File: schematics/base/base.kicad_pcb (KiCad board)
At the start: 2 copper layers, 96.5 x 96.5 mm, 41 parts, among them J1 Bionic_ZIF_Socket_48pin, J2 USB_C_USB2.0_16P, J3 USB_C_USB2.0_16P, J4 P1/P2, J5 P3/P4, J6 P5, J7 P6, SW1 USR_SW, U1 TXS0108EPW, U2 TXS0108EPW, U3 TXS0108EPW, U4 TXS0108EPW, U5 TXS0108EPW, U6 SN74ACT1071DR, U7 SN74ACT1071DR

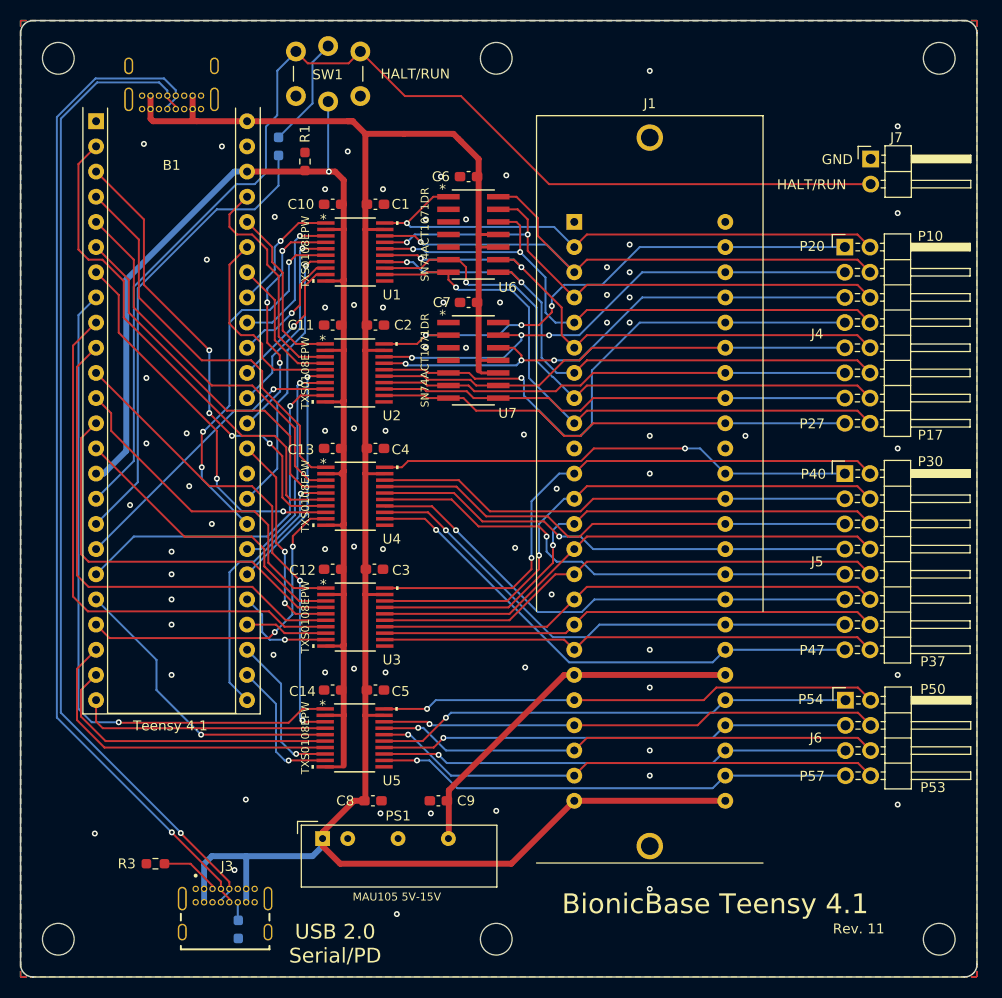
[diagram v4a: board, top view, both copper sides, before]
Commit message: [base] 4 Layers
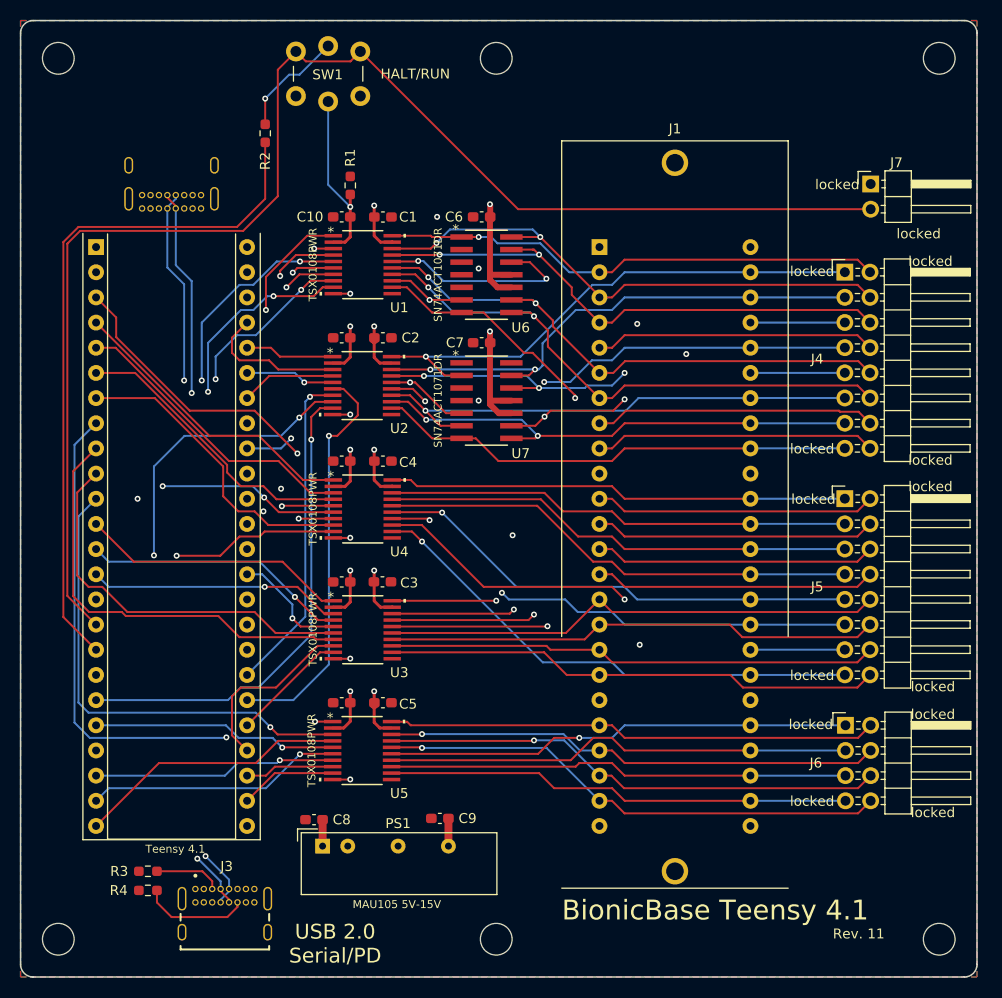
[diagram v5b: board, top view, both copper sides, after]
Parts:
- R2, R4: moved to F.Cu
- moved B1 12.7 mm to (80.7, 64.9)
- moved J2 10.0 mm to (88.3, 56.7)
- moved R4 9.93 mm to (85.9, 129.8), turned to 180 degrees
- moved C8 6.24 mm to (102.7, 122.7), turned to 180 degrees
- moved R1 5.17 mm to (106.3, 58.7)
- moved U7 4.27 mm to (120.1, 80.4)
- moved C7 4.27 mm to (119.6, 74.6)
- moved U6 4.27 mm to (120.1, 67.7)
- moved C6 4.27 mm to (119.6, 61.9)
- moved J1 3.59 mm to (139.1, 78.9)
- moved J4 2.53 mm to (156.2, 67.5)
- moved J5 2.53 mm to (156.2, 90.3)
- moved J6 2.53 mm to (156.3, 113.2)
- moved J7 2.53 mm to (158.9, 58.6)
- moved R2 1.89 mm to (97.7, 53.4)
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- renumbered MH1 to MH2, MH1 to MH3, MH1 to MH4, MH1 to MH5, MH1 to MH6
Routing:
- net Net-(J2-D+-PadA6): track 102.8 -> 74.3 mm, vias 1 -> 2
- net Net-(J2-D--PadA7): track 101.3 -> 74.3 mm, vias 1 -> 2
- net VCC: track 222.2 -> 247.1 mm, vias 0 -> 7
- net Net-(B1-P6.12): track 119.1 -> 143.7 mm
- net +3.3V: track 133.0 -> 156.8 mm, vias 1 -> 10
- net Net-(B1-P6.13): track 47.1 -> 70.4 mm
- net Net-(B1-P6.23): track 13.8 -> 32.3 mm, vias 1 -> 2
- net Net-(B1-P6.19): track 19.8 -> 38.0 mm, vias 1 -> 2
- net Net-(B1-P6.28): track 24.3 -> 41.0 mm
- net Net-(B1-P6.22): track 12.5 -> 28.2 mm, vias 1 -> 2
- net Net-(B1-P6.30): track 29.8 -> 44.2 mm, vias 1 -> 2
- net Net-(B1-P9.07): track 27.9 -> 42.1 mm
- net Net-(B1-P7.02): track 40.8 -> 26.9 mm, vias 0 -> 1
- net Net-(B1-P6.21): track 28.1 -> 41.0 mm
- net Net-(B1-P6.31): track 37.0 -> 49.0 mm
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- added copper zone on In1.Cu, net GND
- added copper zone on In2.Cu, net GND
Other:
- copper layers 2 -> 4
- board text added: "TSX0108PWR"
- board text added: "locked"
- board text removed: "GND"
- board text removed: "P10"
- board text removed: "P17"
- board text removed: "P20"
- board text removed: "P27"
- board text removed: "P30"
- board text removed: "P37"
- board text removed: "P40"
- board text removed: "P47"
- board text removed: "P50"
- board text removed: "P53"
- board text removed: "P54"
- board text removed: "P57"
- board text removed: "TXS0108EPW"

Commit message: [base] Reactor to 2 Layers
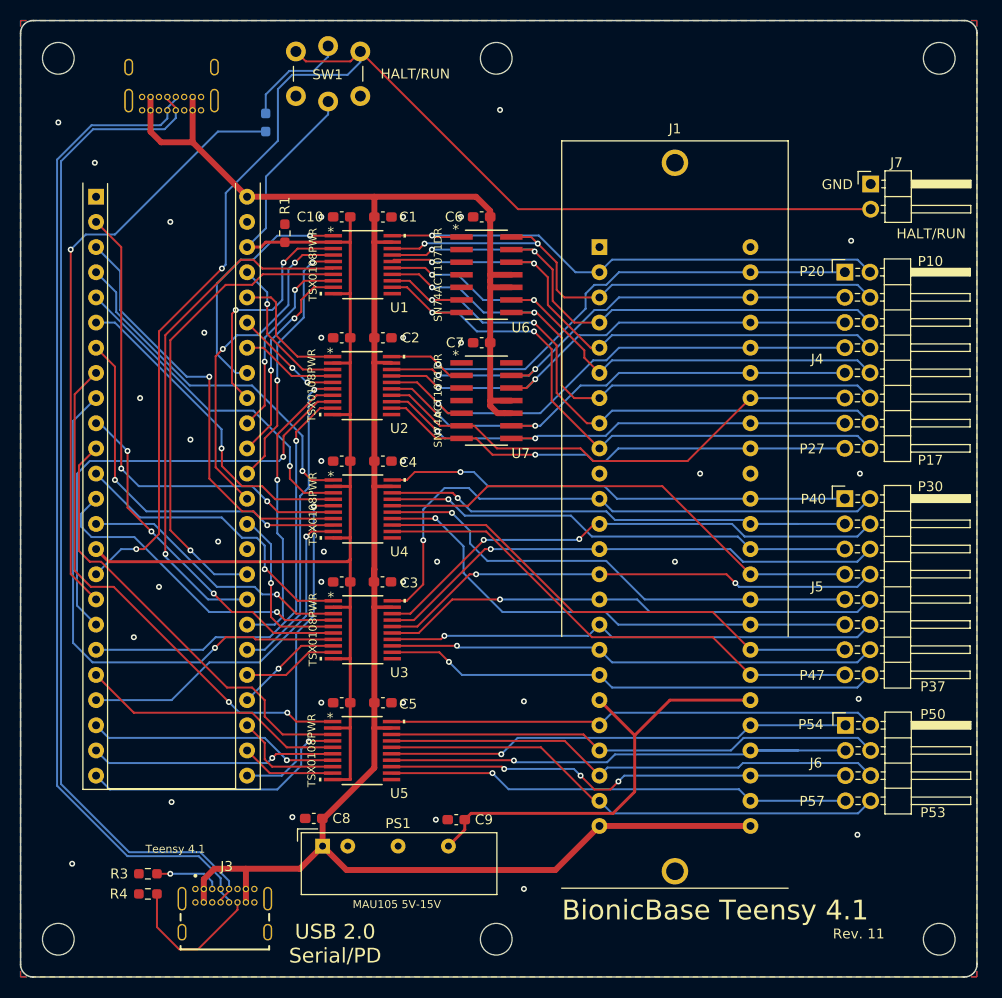
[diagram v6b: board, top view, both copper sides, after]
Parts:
- R2: moved to B.Cu
- moved J2 9.91 mm to (88.3, 46.8)
- moved R1 8.18 mm to (99.7, 63.5)
- moved B1 5.08 mm to (80.7, 59.8)
- moved C9 1.66 mm to (117.0, 122.7)
- moved R2 1.09 mm to (97.8, 52.3)
- moved R4 0.36 mm to (85.9, 130.2)
- moved R3 0.25 mm to (85.9, 128.2)
- moved C8 0.13 mm to (102.7, 122.6)
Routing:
- net +3.3V: track 156.8 -> 127.5 mm, vias 10 -> 0
- net VCC: track 247.1 -> 218.0 mm, vias 7 -> 0
- net Net-(J2-D--PadA7): track 74.3 -> 102.2 mm, vias 2 -> 0
- net Net-(J2-D+-PadA6): track 74.3 -> 101.9 mm, vias 2 -> 0
- net Net-(B1-P6.19): track 38.0 -> 26.3 mm
- net Net-(B1-P6.23): track 32.3 -> 21.1 mm
- net Net-(B1-P7.17): track 43.9 -> 53.9 mm, vias 0 -> 1
- net Net-(B1-P6.12): track 143.7 -> 133.8 mm, vias 0 -> 2
- net Net-(B1-P6.13): track 70.4 -> 61.0 mm, vias 0 -> 1
- net Net-(B1-P6.28): track 41.0 -> 32.0 mm
- net Net-(B1-P6.22): track 28.2 -> 19.7 mm
- net Net-(B1-P9.07): track 42.1 -> 34.0 mm
- net Net-(B1-P6.20): track 45.1 -> 52.9 mm
- net Net-(B1-P9.08): track 31.0 -> 38.1 mm, vias 0 -> 2
- net Net-(B1-P6.21): track 41.0 -> 48.0 mm
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- removed copper zone on In1.Cu, net GND
- removed copper zone on In2.Cu, net GND
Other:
- copper layers 4 -> 2
- board text added: "GND"
- board text added: "P10"
- board text added: "P17"
- board text added: "P20"
- board text added: "P27"
- board text added: "P30"
- board text added: "P37"
- board text added: "P40"
- board text added: "P47"
- board text added: "P50"
- board text added: "P53"
- board text added: "P54"
- board text added: "P57"
- board text removed: "locked"

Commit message: [base] Add power LED and Debug jumper
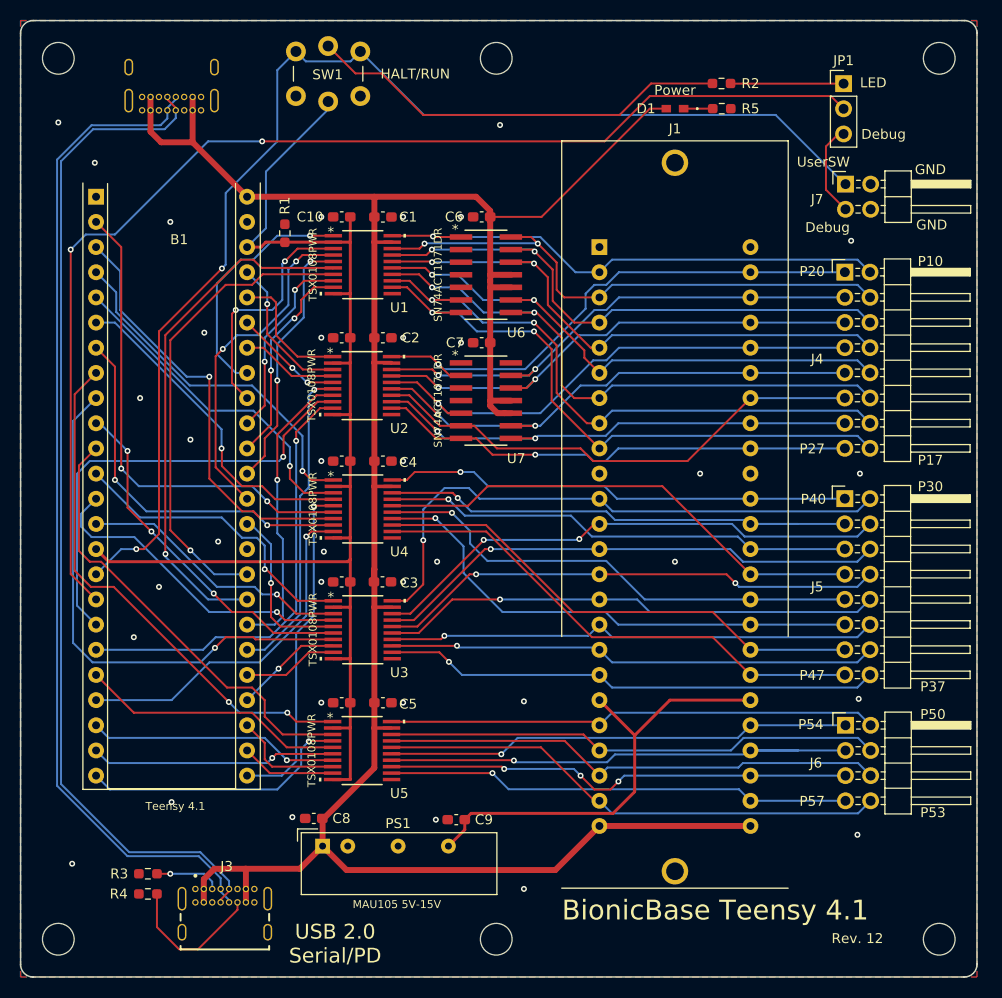
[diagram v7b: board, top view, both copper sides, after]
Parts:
- added D1: CSL1901UW1, 0-LocalLibrary:LED_CSL1901UW1_ROM-M, F.Cu at (139.1, 51.0)
- added JP1: Debug, Connector_PinHeader_2.54mm:PinHeader_1x03_P2.54mm_Vertical, F.Cu at (156.1, 48.4)
- added R5: 1.6k, Resistor_SMD:R_0603_1608Metric_Pad0.98x0.95mm_HandSolder, F.Cu at (143.8, 51.0)
- J7: value P6 -> Debug; footprint Connector_PinHeader_2.54mm:PinHeader_1x02_P2.54mm_Horizontal -> Connector_PinHeader_2.54mm:PinHeader_2x02_P2.54mm_Horizontal
- R2: moved to F.Cu
- moved R2 46.2 mm to (143.8, 48.4), turned to 0 degrees
- moved J7 2.55 mm to (156.3, 58.6)
- moved U6 0.05 mm to (120.0, 67.7)
- moved U7 0.05 mm to (120.0, 80.4)
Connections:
- J7 pad 1: GND -> Net-(B1-P6.12)
- J7 pad 2: Net-(B1-P6.12) -> GND
- R2 pad 2: Net-(B1-P6.13) -> Net-(JP1-A)
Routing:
- net Net-(B1-P6.13): track 61.0 -> 122.1 mm, vias 1 -> 2
- net Net-(SW1-K): track 10.9 -> 43.0 mm
- net VCC: track 218.0 -> 240.2 mm
- net Net-(JP1-A): track 0.00 -> 11.4 mm
- net Net-(B1-P6.12): track 133.8 -> 124.3 mm
- net Net-(J7-Pin_3): track 0.00 -> 9.45 mm
- net Net-(D1-K): track 0.00 -> 2.93 mm
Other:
- board text added: "Debug"
- board text added: "LED"
- board text added: "Power"
- board text added: "Rev. 12"
- board text added: "UserSW"
- board text removed: "Rev. 11"
